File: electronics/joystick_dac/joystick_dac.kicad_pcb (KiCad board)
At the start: 2 copper layers, 51 x 21 mm, 0 parts

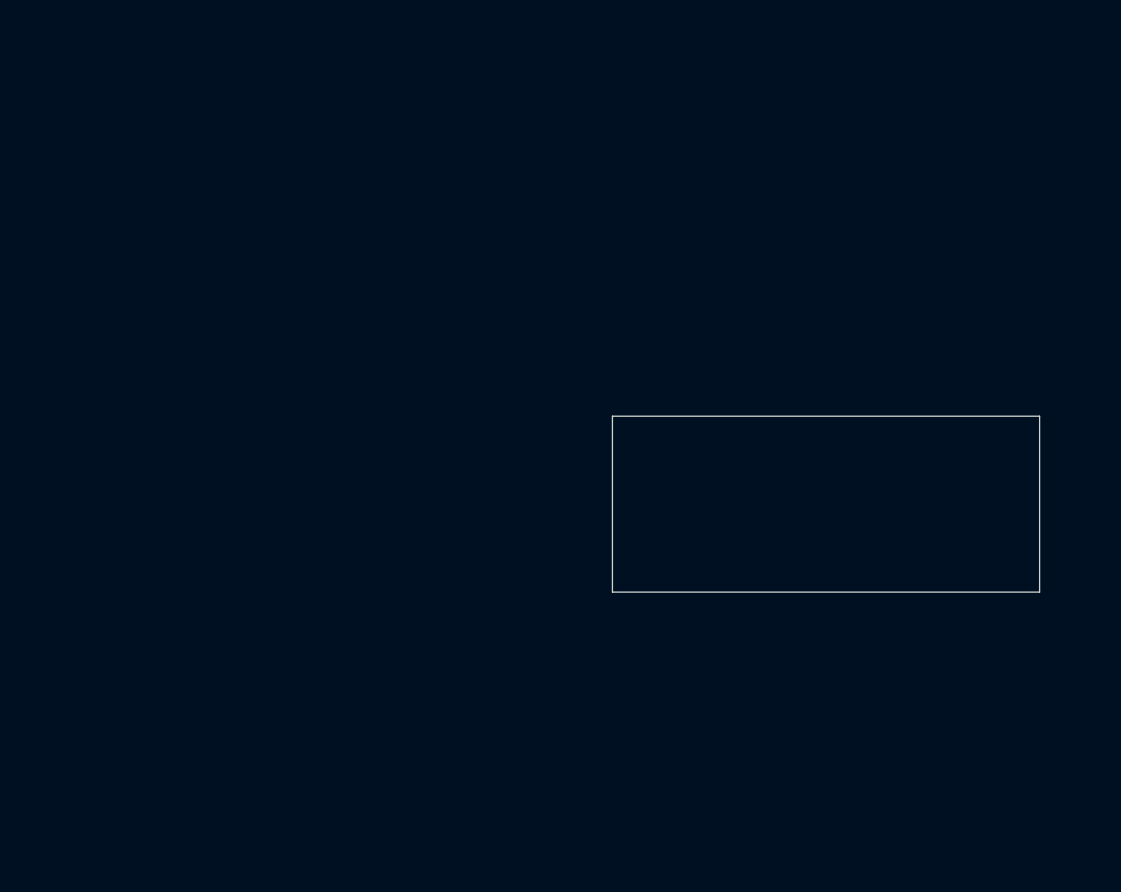
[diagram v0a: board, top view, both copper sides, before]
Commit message: quick prototype of dac board for joystick
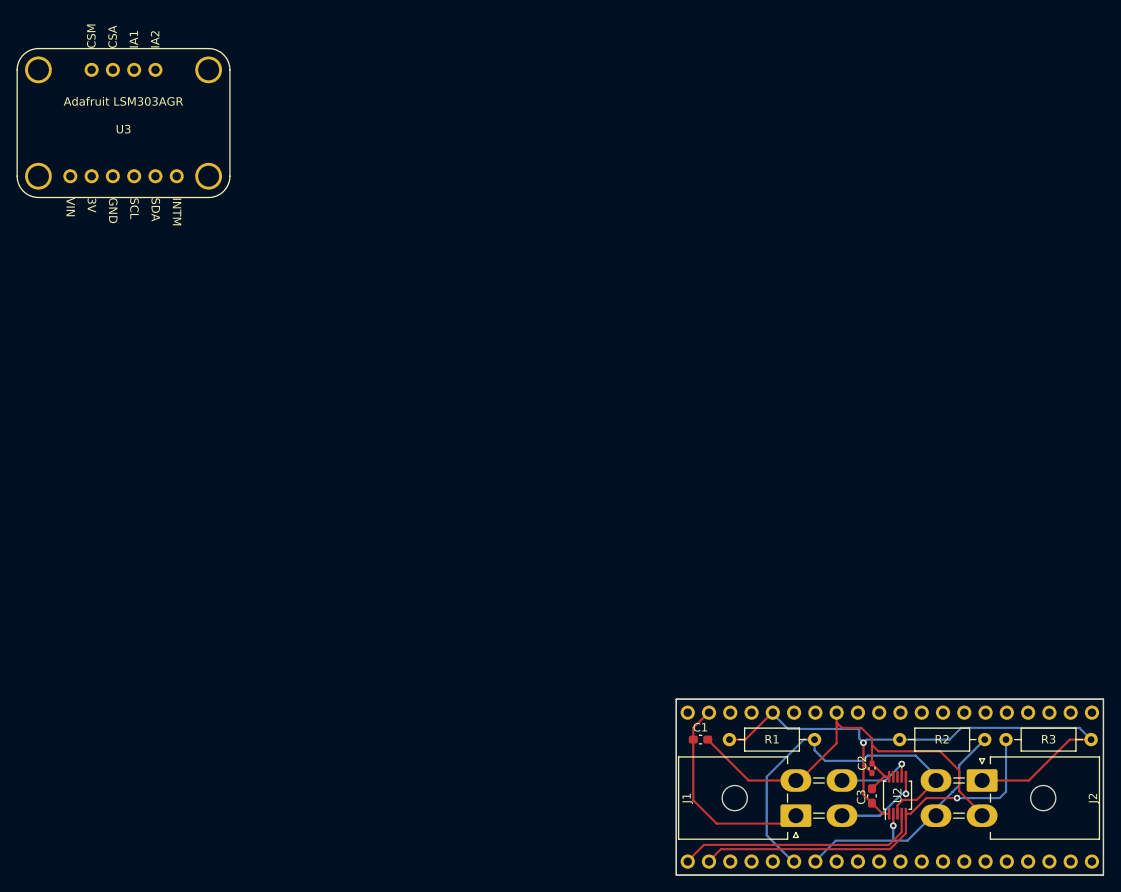
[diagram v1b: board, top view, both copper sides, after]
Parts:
- added C1: 10u, Capacitor_SMD:C_0603_1608Metric_Pad1.08x0.95mm_HandSolder, F.Cu at (81.6, 82.5)
- added C2: 0.1u, Capacitor_SMD:C_0402_1005Metric_Pad0.74x0.62mm_HandSolder, F.Cu at (102.1, 86.0)
- added C3: 10u, Capacitor_SMD:C_0603_1608Metric_Pad1.08x0.95mm_HandSolder, F.Cu at (102.1, 89.3)
- added J1: Power/Signal Out, Connector_Molex:Molex_Mini-Fit_Jr_5569-04A2_2x02_P4.20mm_Horizontal, F.Cu at (93.0, 91.6)
- added J2: Magnetometer, Connector_Molex:Molex_Mini-Fit_Jr_5569-04A2_2x02_P4.20mm_Horizontal, F.Cu at (115.3, 87.4)
- added R1: 4K7, Resistor_THT:R_Axial_DIN0207_L6.3mm_D2.5mm_P10.16mm_Horizontal, F.Cu at (85.1, 82.5)
- added R2: 4K7, Resistor_THT:R_Axial_DIN0207_L6.3mm_D2.5mm_P10.16mm_Horizontal, F.Cu at (105.4, 82.5)
- added R3: 100K, Resistor_THT:R_Axial_DIN0207_L6.3mm_D2.5mm_P10.16mm_Horizontal, F.Cu at (118.1, 82.5)
- added U1: raspberry_pi_pico, custom_parts:raspberry_pi_pico, F.Cu at (103.0, 88.6)
- added U2: MCP4728, Package_SO:MSOP-10_3x3mm_P0.5mm, F.Cu at (105.2, 89.2)
- added U3: ~, custom_parts:adafruit_lsm303agr, F.Cu at (12.8, 10.2)
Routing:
- net /+3V3_2: track 0.00 -> 74.6 mm, vias 0 -> 1
- net GND: track 0.00 -> 53.8 mm
- net Net-(U1-GP1): track 0.00 -> 46.6 mm, vias 0 -> 1
- net /SDA: track 0.00 -> 43.8 mm
- net /SCL: track 0.00 -> 31.1 mm, vias 0 -> 1
- net Net-(U1-GP0): track 0.00 -> 29.3 mm
- net /+3V3: track 0.00 -> 25.0 mm
- net /JoystickX: track 0.00 -> 10.8 mm, vias 0 -> 1
- net /JoystickY: track 0.00 -> 9.49 mm, vias 0 -> 1

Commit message: work on integrated joystick pcb thing
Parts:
- removed U3: ~, custom_parts:adafruit_lsm303agr
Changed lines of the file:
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@@
   (net 43 "unconnected-(U2-VOUTC-Pad8)")
   (net 44 "unconnected-(U2-VOUTD-Pad9)")
-  (net 45 "unconnected-(U3-CSM-Pad0)")
-  (net 46 "unconnected-(U3-CSA-Pad1)")
-  (net 47 "unconnected-(U3-IA1-Pad2)")
-  (net 48 "unconnected-(U3-IA2-Pad3)")
-  (net 49 "unconnected-(U3-VIN-Pad4)")
-  (net 50 "unconnected-(U3-3V-Pad5)")
-  (net 51 "unconnected-(U3-GND-Pad6)")
-  (net 52 "unconnected-(U3-SCL-Pad7)")
-  (net 53 "unconnected-(U3-SDA-Pad8)")
-  (net 54 "unconnected-(U3-INTM-Pad9)")
   (footprint "Resistor_THT:R_Axial_DIN0207_L6.3mm_D2.5mm_P10.16mm_Horizontal" (layer "F.Cu")
     (at 118.11 82.55)
@@
     )
   )
-  (footprint "custom_parts:adafruit_lsm303agr" (layer "F.Cu")
-    (at 12.75 10.21)
-    (property "Sheetfile" "joystick_dac.kicad_sch")
-    (property "Sheetname" "")
-    (attr through_hole)
-    (fp_text reference "U3" (at 0 -0.5 unlocked) (layer "F.SilkS")
-        (effects (font (size 1 1) (thickness 0.1)))
-    )
-    (fp_text value "~" (at 0 1 unlocked) (layer "F.Fab")
-        (effects (font (size 1 1) (thickness 0.15)))
-    )
-    (fp_text user "Adafruit LSM303AGR" (at 0 -3.81 unlocked) (layer "F.SilkS")
-        (effects (font (size 1 1) (thickness 0.1)))
-    )
-    (fp_text user "SDA" (at 3.81 7.62 270 unlocked) (layer "F.SilkS")
-        (effects (font (size 1 1) (thickness 0.1)) (justify left))
-    )
-    (fp_text user "IA1" (at 1.27 -10.16 90 unlocked) (layer "F.SilkS")
-        (effects (font (size 1 1) (thickness 0.1)) (justify left))
-    )
-    (fp_text user "SCL" (at 1.27 7.62 270 unlocked) (layer "F.SilkS")
-        (effects (font (size 1 1) (thickness 0.1)) (justify left))
-    )
-    (fp_text user "GND" (at -1.27 7.62 270 unlocked) (layer "F.SilkS")
-        (effects (font (size 1 1) (thickness 0.1)) (justify left))
-    )
-    (fp_text user "VIN" (at -6.35 7.62 270 unlocked) (layer "F.SilkS")
-        (effects (font (size 1 1) (thickness 0.1)) (justify left))
-    )
-    (fp_text user "INTM" (at 6.35 7.62 270 unlocked) (layer "F.SilkS")
-        (effects (font (size 1 1) (thickness 0.1)) (justify left))
-    )
-    (fp_text user "CSM" (at -3.81 -10.16 90 unlocked) (layer "F.SilkS")
-        (effects (font (size 1 1) (thickness 0.1)) (justify left))
-    )
-    (fp_text user "IA2" (at 3.81 -10.16 90 unlocked) (layer "F.SilkS")
-        (effects (font (size 1 1) (thickness 0.1)) (justify left))
-    )
-    (fp_text user "CSA" (at -1.27 -10.16 90 unlocked) (layer "F.SilkS")
-        (effects (font (size 1 1) (thickness 0.1)) (justify left))
-    )
-    (fp_text user "3V" (at -3.81 7.62 270 unlocked) (layer "F.SilkS")
-        (effects (font (size 1 1) (thickness 0.1)) (justify left))
-    )
-    (fp_text user "${REFERENCE}" (at 0 2.5 unlocked) (layer "F.Fab")
-        (effects (font (size 1 1) (thickness 0.15)))
-    )
-    (fp_line (start -12.7 5.08) (end -12.7 -7.62)
-      (stroke (width 0.1) (type default)) (layer "F.SilkS"))
-    (fp_line (start -10.16 -10.16) (end 10.16 -10.16)
-      (stroke (width 0.1) (type default)) (layer "F.SilkS"))
-    (fp_line (start -10.16 7.62) (end 10.16 7.62)
-      (stroke (width 0.1) (type default)) (layer "F.SilkS"))
-    (fp_line (start 12.7 5.08) (end 12.7 -7.62)
-      (stroke (width 0.1) (type default)) (layer "F.SilkS"))
-    (fp_arc (start -12.7 -7.62) (mid -11.956051 -9.416051) (end -10.16 -10.16)
-      (stroke (width 0.1) (type default)) (layer "F.SilkS"))
-    (fp_arc (start -10.16 7.62) (mid -11.956051 6.876051) (end -12.7 5.08)
-      (stroke (width 0.1) (type default)) (layer "F.SilkS"))
-    (fp_arc (start 10.16 -10.16) (mid 11.956051 -9.416051) (end 12.7 -7.62)
-      (stroke (width 0.1) (type default)) (layer "F.SilkS"))
-    (fp_arc (start 12.7 5.08) (mid 11.956051 6.876051) (end 10.16 7.62)
-      (stroke (width 0.1) (type default)) (layer "F.SilkS"))
-    (pad "" thru_hole circle (at -10.16 -7.62) (size 3.2 3.2) (drill 2.5) (layers "*.Cu" "*.Mask")
-      (zone_connect 0))
-    (pad "" thru_hole circle (at -10.16 5.08) (size 3.2 3.2) (drill 2.5) (layers "*.Cu" "*.Mask")
-      (zone_connect 0))
-    (pad "" thru_hole circle (at 10.16 -7.62) (size 3.2 3.2) (drill 2.5) (layers "*.Cu" "*.Mask")
-      (zone_connect 0))
-    (pad "" thru_hole circle (at 10.16 5.08) (size 3.2 3.2) (drill 2.5) (layers "*.Cu" "*.Mask")
-      (zone_connect 0))
-    (pad "0" thru_hole circle (at -3.81 -7.62 90) (size 1.6764 1.6764) (drill 1) (layers "*.Cu" "*.Mask")
-      (net 45 "unconnected-(U3-CSM-Pad0)") (pinfunction "CSM") (pintype "bidirectional"))
-    (pad "1" thru_hole circle (at -1.27 -7.62 90) (size 1.6764 1.6764) (drill 1) (layers "*.Cu" "*.Mask")
-      (net 46 "unconnected-(U3-CSA-Pad1)") (pinfunction "CSA") (pintype "bidirectional"))
-    (pad "2" thru_hole circle (at 1.27 -7.62 90) (size 1.6764 1.6764) (drill 1) (layers "*.Cu" "*.Mask")
-      (net 47 "unconnected-(U3-IA1-Pad2)") (pinfunction "IA1") (pintype "bidirectional"))
-    (pad "3" thru_hole circle (at 3.81 -7.62 90) (size 1.6764 1.6764) (drill 1) (layers "*.Cu" "*.Mask")
-      (net 48 "unconnected-(U3-IA2-Pad3)") (pinfunction "IA2") (pintype "bidirectional"))
-    (pad "4" thru_hole circle (at -6.35 5.08 90) (size 1.6764 1.6764) (drill 1) (layers "*.Cu" "*.Mask")
-      (net 49 "unconnected-(U3-VIN-Pad4)") (pinfunction "VIN") (pintype "bidirectional"))
-    (pad "5" thru_hole circle (at -3.81 5.08 90) (size 1.6764 1.6764) (drill 1) (layers "*.Cu" "*.Mask")
-      (net 50 "unconnected-(U3-3V-Pad5)") (pinfunction "3V") (pintype "output"))
-    (pad "6" thru_hole circle (at -1.27 5.08 90) (size 1.6764 1.6764) (drill 1) (layers "*.Cu" "*.Mask")
-      (net 51 "unconnected-(U3-GND-Pad6)") (pinfunction "GND") (pintype "bidirectional"))
-    (pad "7" thru_hole circle (at 1.27 5.08 90) (size 1.6764 1.6764) (drill 1) (layers "*.Cu" "*.Mask")
-      (net 52 "unconnected-(U3-SCL-Pad7)") (pinfunction "SCL") (pintype "bidirectional"))
-    (pad "8" thru_hole circle (at 3.81 5.08 90) (size 1.6764 1.6764) (drill 1) (layers "*.Cu" "*.Mask")
-      (net 53 "unconnected-(U3-SDA-Pad8)") (pinfunction "SDA") (pintype "bidirectional"))
-    (pad "9" thru_hole circle (at 6.35 5.08 90) (size 1.6764 1.6764) (drill 1) (layers "*.Cu" "*.Mask")
-      (net 54 "unconnected-(U3-INTM-Pad9)") (pinfunction "INTM") (pintype "bidirectional"))
-  )
   (footprint "Connector_Molex:Molex_Mini-Fit_Jr_5569-04A2_2x02_P4.20mm_Horizontal" (layer "F.Cu")
